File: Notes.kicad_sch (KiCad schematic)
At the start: 0 parts

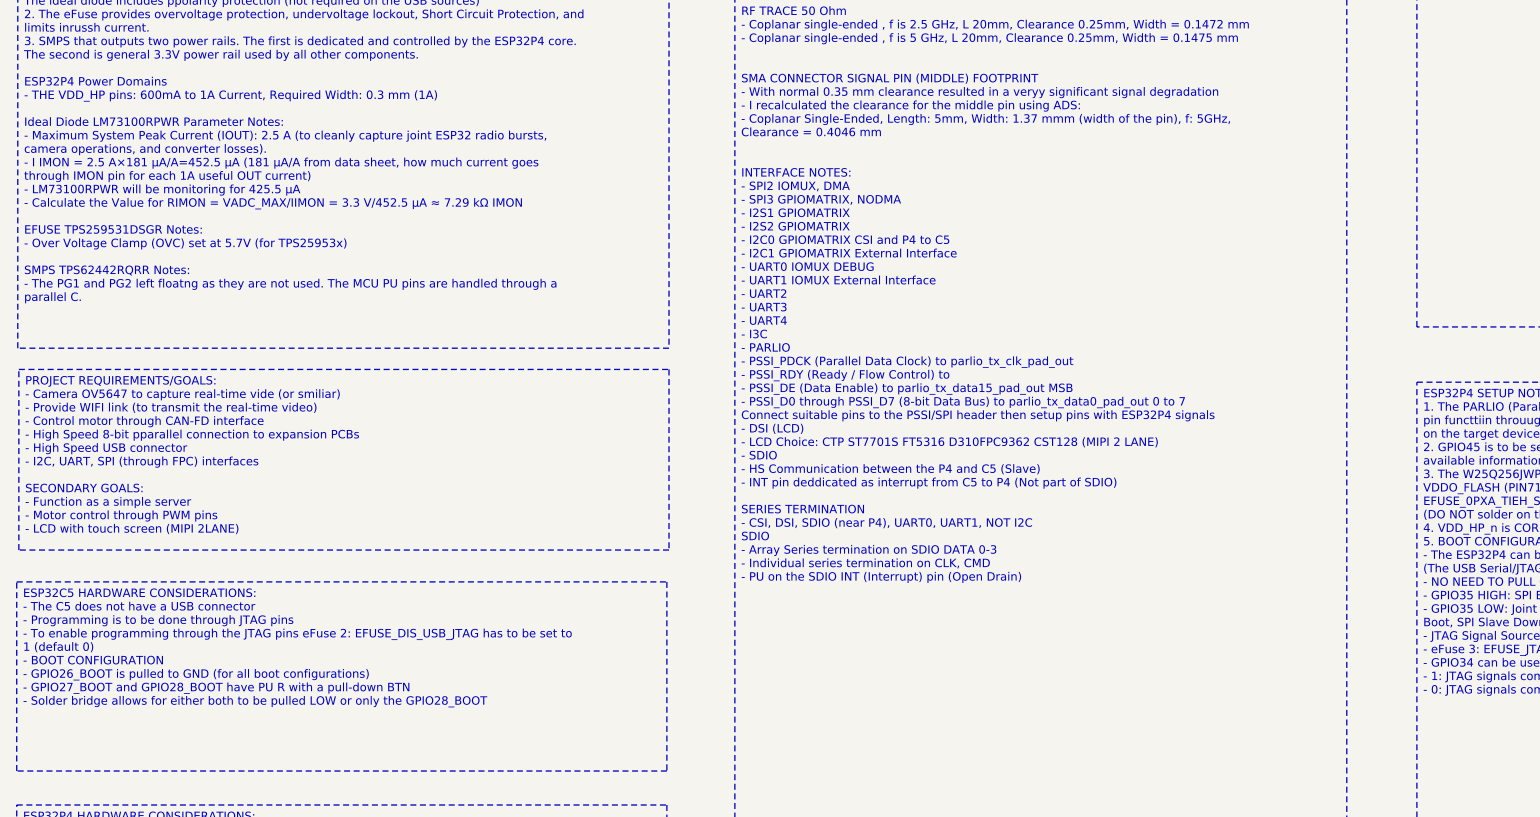
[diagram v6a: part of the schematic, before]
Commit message: Power Rail Update
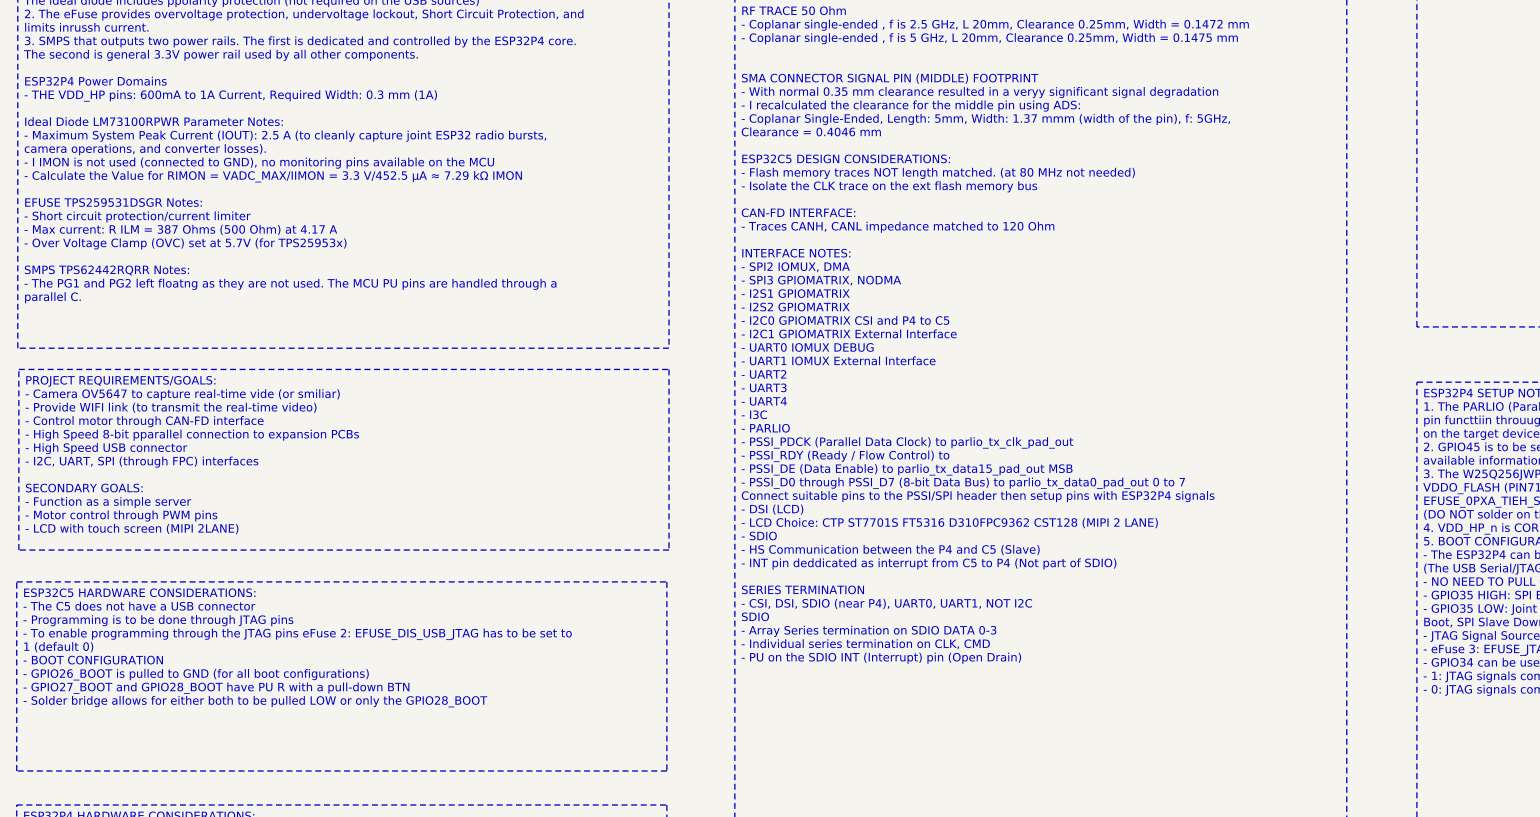
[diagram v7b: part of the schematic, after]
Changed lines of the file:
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@@
 		(company "Peter Hancak")
 	)
-	(text_box "CONTROLLED IMPEDANCE TRACE WIDTHS\n(Simulations done using ADS Controlled Impedance Line Designer)\n- Simulated is JLCPCB: JLC04161H-3313(Finished thickness1.56mm±10%)\n\n1. Microstrip Edge Coupled, 100 Ohm Differential Impedance, 0.35mm (center to center), 50mmm Length, f=1Ghz, Width = 0.1225 mm\n2. Coplanar Edge Coupled, 100 Ohm Differential Impedance, 0.35mm (center to center), 0.25mm Clearance, 50mmm Length, f=1Ghz, Width = 0.1354 mm, 0.35 - 0.1354 = 0.2146 mm (edge to edge spacing)\n3. USB Coplanar Edge Coupled, 90 Ohm Differential Impedance, 0.5mm (center to center), 0.25mm Clearance, 50mmm Length, f=240Mhz, Width = 0.1704 mm, 0.5 - 0.1704 = 0.3296 mm\n4. USB Microstrip Edge Coupled, 90 Ohm Differential Impedance, 0.5mm (center to center), 50mmm Length, f=240Mhz, Width = 0.1722 mm\n\nRF TRACE 50 Ohm\n- Coplanar single-ended , f is 2.5 GHz, L 20mm, Clearance 0.25mm, Width = 0.1472 mm\n- Coplanar single-ended , f is 5 GHz, L 20mm, Clearance 0.25mm, Width = 0.1475 mm\n\n\nSMA CONNECTOR SIGNAL PIN (MIDDLE) FOOTPRINT\n- With normal 0.35 mm clearance resulted in a veryy significant signal degradation\n- I recalculated the clearance for the middle pin using ADS:\n  - Coplanar Single-Ended, Length: 5mm, Width: 1.37 mmm (width of the pin), f: 5GHz, Clearance = 0.4046 mm\n  \n\nINTERFACE NOTES:\n- SPI2 IOMUX, DMA\n- SPI3 GPIOMATRIX, NODMA\n- I2S1 GPIOMATRIX\n- I2S2 GPIOMATRIX\n- I2C0 GPIOMATRIX CSI and P4 to C5\n- I2C1 GPIOMATRIX External Interface\n- UART0 IOMUX DEBUG\n- UART1 IOMUX External Interface\n- UART2\n- UART3\n- UART4\n- I3C\n- PARLIO\n  - PSSI_PDCK (Parallel Data Clock) to parlio_tx_clk_pad_out\n  - PSSI_RDY (Ready / Flow Control) to \n  - PSSI_DE (Data Enable) to parlio_tx_data15_pad_out MSB\n  - PSSI_D0 through PSSI_D7 (8-bit Data Bus) to parlio_tx_data0_pad_out 0 to 7\n  Connect suitable pins to the PSSI/SPI header then setup pins with ESP32P4 signals\n- DSI (LCD)\n  - LCD Choice: CTP ST7701S FT5316 D310FPC9362 CST128 (MIPI 2 LANE)\n- SDIO\n  - HS Communication between the P4 and C5 (Slave)\n  - INT pin deddicated as interrupt from C5 to P4 (Not part of SDIO)\n\nSERIES TERMINATION\n- CSI, DSI, SDIO (near P4), UART0, UART1, NOT I2C\nSDIO\n- Array Series termination on SDIO DATA 0-3\n- Individual series termination on CLK, CMD\n- PU on the SDIO INT (Interrupt) pin (Open Drain)"
+	(text_box "CONTROLLED IMPEDANCE TRACE WIDTHS\n(Simulations done using ADS Controlled Impedance Line Designer)\n- Simulated is JLCPCB: JLC04161H-3313(Finished thickness1.56mm±10%)\n\n1. Microstrip Edge Coupled, 100 Ohm Differential Impedance, 0.35mm (center to center), 50mmm Length, f=1Ghz, Width = 0.1225 mm\n2. Coplanar Edge Coupled, 100 Ohm Differential Impedance, 0.35mm (center to center), 0.25mm Clearance, 50mmm Length, f=1Ghz, Width = 0.1354 mm, 0.35 - 0.1354 = 0.2146 mm (edge to edge spacing)\n3. USB Coplanar Edge Coupled, 90 Ohm Differential Impedance, 0.5mm (center to center), 0.25mm Clearance, 50mmm Length, f=240Mhz, Width = 0.1704 mm, 0.5 - 0.1704 = 0.3296 mm\n4. USB Microstrip Edge Coupled, 90 Ohm Differential Impedance, 0.5mm (center to center), 50mmm Length, f=240Mhz, Width = 0.1722 mm\n\nRF TRACE 50 Ohm\n- Coplanar single-ended , f is 2.5 GHz, L 20mm, Clearance 0.25mm, Width = 0.1472 mm\n- Coplanar single-ended , f is 5 GHz, L 20mm, Clearance 0.25mm, Width = 0.1475 mm\n\n\nSMA CONNECTOR SIGNAL PIN (MIDDLE) FOOTPRINT\n- With normal 0.35 mm clearance resulted in a veryy significant signal degradation\n- I recalculated the clearance for the middle pin using ADS:\n  - Coplanar Single-Ended, Length: 5mm, Width: 1.37 mmm (width of the pin), f: 5GHz, Clearance = 0.4046 mm\n\nESP32C5 DESIGN CONSIDERATIONS:\n- Flash memory traces NOT length matched. (at 80 MHz not needed)\n- Isolate the CLK trace on the ext flash memory bus\n\nCAN-FD INTERFACE:\n- Traces CANH, CANL impedance matched to 120 Ohm\n\nINTERFACE NOTES:\n- SPI2 IOMUX, DMA\n- SPI3 GPIOMATRIX, NODMA\n- I2S1 GPIOMATRIX\n- I2S2 GPIOMATRIX\n- I2C0 GPIOMATRIX CSI and P4 to C5\n- I2C1 GPIOMATRIX External Interface\n- UART0 IOMUX DEBUG\n- UART1 IOMUX External Interface\n- UART2\n- UART3\n- UART4\n- I3C\n- PARLIO\n  - PSSI_PDCK (Parallel Data Clock) to parlio_tx_clk_pad_out\n  - PSSI_RDY (Ready / Flow Control) to \n  - PSSI_DE (Data Enable) to parlio_tx_data15_pad_out MSB\n  - PSSI_D0 through PSSI_D7 (8-bit Data Bus) to parlio_tx_data0_pad_out 0 to 7\n  Connect suitable pins to the PSSI/SPI header then setup pins with ESP32P4 signals\n- DSI (LCD)\n  - LCD Choice: CTP ST7701S FT5316 D310FPC9362 CST128 (MIPI 2 LANE)\n- SDIO\n  - HS Communication between the P4 and C5 (Slave)\n  - INT pin deddicated as interrupt from C5 to P4 (Not part of SDIO)\n\nSERIES TERMINATION\n- CSI, DSI, SDIO (near P4), UART0, UART1, NOT I2C\nSDIO\n- Array Series termination on SDIO DATA 0-3\n- Individual series termination on CLK, CMD\n- PU on the SDIO INT (Interrupt) pin (Open Drain)"
 		(exclude_from_sim no)
 		(at 113.03 29.464 0)
@@
 		)
 	)
-	(text_box "POWER MANAGEMENT NOTES:\n- The input power goes through three stages \n  1. a) External Power: LM73100RPWR, 2.7 - 23 V, 5.5 A Integrated Ideal Diode with Input Reverse Polarity and Overvoltage Protection\n     b) USB POWER: SS34-E3/57T Diode\n  2. TPS259531DSGR 2.7V to 18V, 4-A, 34-mΩ eFuse With Fast Overvoltage Protection\n  3. TPS62442RQRR, 2.75-V to 6-V, Dual-Channel Step-Down Converter with Adjustable Frequency\n\n- Stage Description:\n  1. The power is sourced from the imediatelly connected power source without relying on jumpers to manual selection. The diodes prevent current from flowing back to a source in case of multiple ppower sources being conected.\n     The ideal diode was used for thhe external power source to limit power loss inherent in a regular diode as the eternal power source will at times be a battery.   \n     The ideal diode includes ppolarity protection (not required on the USB sources)\n  2. The eFuse provides overvoltage protection, undervoltage lockout, Short Circuit Protection, and limits inrussh current.\n  3. SMPS that outputs two power rails. The first is dedicated and controlled by the ESP32P4 core. The second is general 3.3V power rail used by all other components.\n\nESP32P4 Power Domains\n- THE VDD_HP pins: 600mA to 1A Current, Required Width: 0.3 mm (1A)\n\nIdeal Diode LM73100RPWR Parameter Notes:\n- Maximum System Peak Current (IOUT): 2.5 A (to cleanly capture joint ESP32 radio bursts, camera operations, and converter losses).\n- I IMON = 2.5 A×181 μA/A=452.5 μA (181 μA/A from data sheet, how much current goes through IMON pin for each 1A useful OUT current)  \n- LM73100RPWR will be monitoring for 425.5 μA\n- Calculate the Value for RIMON = VADC_MAX/IIMON = 3.3 V/452.5 μA ≈ 7.29 kΩ IMON\n​\nEFUSE TPS259531DSGR Notes:\n- Over Voltage Clamp (OVC) set at 5.7V (for TPS25953x)\n\nSMPS TPS62442RQRR Notes:\n- The PG1 and PG2 left floatng as they are not used. The MCU PU pins are handled through a parallel C. \n"
+	(text_box "POWER MANAGEMENT NOTES:\n- The input power goes through three stages \n  1. a) External Power: LM73100RPWR, 2.7 - 23 V, 5.5 A Integrated Ideal Diode with Input Reverse Polarity and Overvoltage Protection\n     b) USB POWER: SS34-E3/57T Diode\n  2. TPS259531DSGR 2.7V to 18V, 4-A, 34-mΩ eFuse With Fast Overvoltage Protection\n  3. TPS62442RQRR, 2.75-V to 6-V, Dual-Channel Step-Down Converter with Adjustable Frequency\n\n- Stage Description:\n  1. The power is sourced from the imediatelly connected power source without relying on jumpers to manual selection. The diodes prevent current from flowing back to a source in case of multiple ppower sources being conected.\n     The ideal diode was used for thhe external power source to limit power loss inherent in a regular diode as the eternal power source will at times be a battery.   \n     The ideal diode includes ppolarity protection (not required on the USB sources)\n  2. The eFuse provides overvoltage protection, undervoltage lockout, Short Circuit Protection, and limits inrussh current.\n  3. SMPS that outputs two power rails. The first is dedicated and controlled by the ESP32P4 core. The second is general 3.3V power rail used by all other components.\n\nESP32P4 Power Domains\n- THE VDD_HP pins: 600mA to 1A Current, Required Width: 0.3 mm (1A)\n\nIdeal Diode LM73100RPWR Parameter Notes:\n- Maximum System Peak Current (IOUT): 2.5 A (to cleanly capture joint ESP32 radio bursts, camera operations, and converter losses).\n- I IMON is not used (connected to GND), no monitoring pins available on the MCU\n- Calculate the Value for RIMON = VADC_MAX/IIMON = 3.3 V/452.5 μA ≈ 7.29 kΩ IMON\n​\nEFUSE TPS259531DSGR Notes:\n- Short circuit protection/current limiter\n- Max current: R ILM = 387 Ohms (500 Ohm) at 4.17 A\n- Over Voltage Clamp (OVC) set at 5.7V (for TPS25953x)\n\nSMPS TPS62442RQRR Notes:\n- The PG1 and PG2 left floatng as they are not used. The MCU PU pins are handled through a parallel C. \n"
 		(exclude_from_sim no)
 		(at 27.305 29.845 0)
